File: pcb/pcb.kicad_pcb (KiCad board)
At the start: 2 copper layers, 168.9 x 103.7 mm, 129 parts, among them J1 MJ-4PP-9, J2 MJ-4PP-9, J3 USB_C_Receptacle_USB2.0_16P, J4 USB to TTL, J5 Conn_01x03, J6 Conn_01x03, SW1 KEY_SW, SW10 KEY_SW, SW11 KEY_SW, SW12 KEY_SW, SW13 KEY_SW, SW14 KEY_SW, SW15 KEY_SW, SW16 KEY_SW, SW17 KEY_SW, SW18 KEY_SW, SW19 KEY_SW, SW2 KEY_SW, SW20 KEY_SW, SW21 KEY_SW, SW22 KEY_SW, SW23 KEY_SW, SW24 KEY_SW, SW25 KEY_SW, SW26 KEY_SW, SW27 RotaryEncoder, SW3 KEY_SW, SW30 KEY_SW, SW31 KEY_SW, SW32 KEY_SW, SW33 KEY_SW, SW34 KEY_SW, SW35 KEY_SW, SW36 KEY_SW, SW37 KEY_SW, SW38 KEY_SW, SW39 KEY_SW, SW4 KEY_SW, SW40 KEY_SW, SW41 KEY_SW, SW42 KEY_SW, SW43 KEY_SW, SW44 KEY_SW, SW45 KEY_SW, SW46 KEY_SW, SW47 KEY_SW, SW48 KEY_SW, SW49 KEY_SW, SW5 KEY_SW, SW50 KEY_SW, SW51 KEY_SW, SW52 KEY_SW, SW53 KEY_SW, SW54 KEY_SW, SW6 KEY_SW, SW60 RESET_SW, SW61 BOOT_SW, SW7 KEY_SW, SW8 KEY_SW, SW9 KEY_SW, SW６２1 DIP_SW, U1 ESP32-S3-WROOM-1, U2 TPS1117LV33S, U3 USBLC6-2SC6

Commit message: ortder pcb
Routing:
- net GND: vias 39 -> 45
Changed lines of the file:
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@@
 		(allow_soldermask_bridges_in_footprints no)
 		(aux_axis_origin 232.454776 63.317318)
-		(grid_origin 108.645 50.033114)
+		(grid_origin 111.684776 43.117318)
 		(pcbplotparams
 			(layerselection 0x00010fc_ffffffff)
@@
 			(drillshape 0)
 			(scaleselection 1)
-			(outputdirectory "/home/sotaro/Downloads/")
+			(outputdirectory "../voidaster/")
 		)
 	)
@@
 		(layer "B.SilkS")
 	)
+	(gr_rect
+		(start 107.214776 43.117318)
+		(end 116.154776 50.467318)
+		(stroke
+			(width 0.1)
+			(type solid)
+		)
+		(fill solid)
+		(layer "B.SilkS")
+	)
 	(gr_line
 		(start 180.915 75.502511)
@@
 		(layer "B.SilkS")
 	)
+	(gr_rect
+		(start 107.214776 43.117318)
+		(end 116.154776 50.467318)
+		(stroke
+			(width 0.1)
+			(type solid)
+		)
+		(fill solid)
+		(layer "F.SilkS")
+	)
 	(gr_line
 		(start 124.67977 72.692318)
@@
 	)
 	(via
+		(at 132.174776 51.637318)
+		(size 0.6)
+		(drill 0.3)
+		(layers "F.Cu" "B.Cu")
+		(free yes)
+		(net 34)
+	)
+	(via
 		(at 194.455 95.713114)
 		(size 0.6)
@@
 	)
 	(via
+		(at 165.704776 51.767318)
+		(size 0.6)
+		(drill 0.3)
+		(layers "F.Cu" "B.Cu")
+		(free yes)
+		(net 34)
+	)
+	(via
 		(at 165.885 108.353114)
 		(size 0.6)
@@
 	)
 	(via
+		(at 169.734776 51.747318)
+		(size 0.6)
+		(drill 0.3)
+		(layers "F.Cu" "B.Cu")
+		(free yes)
+		(net 34)
+	)
+	(via
+		(at 137.284776 51.637318)
+		(size 0.6)
+		(drill 0.3)
+		(layers "F.Cu" "B.Cu")
+		(free yes)
+		(net 34)
+	)
+	(via
 		(at 118.035 115.043114)
 		(size 0.6)
@@
 		(net 34)
 	)
+	(via
+		(at 127.774776 51.577318)
+		(size 0.6)
+		(drill 0.3)
+		(layers "F.Cu" "B.Cu")
+		(free yes)
+		(net 34)
+	)
+	(via
+		(at 162.124776 51.837318)
+		(size 0.6)
+		(drill 0.3)
+		(layers "F.Cu" "B.Cu")
+		(free yes)
+		(net 34)
+	)

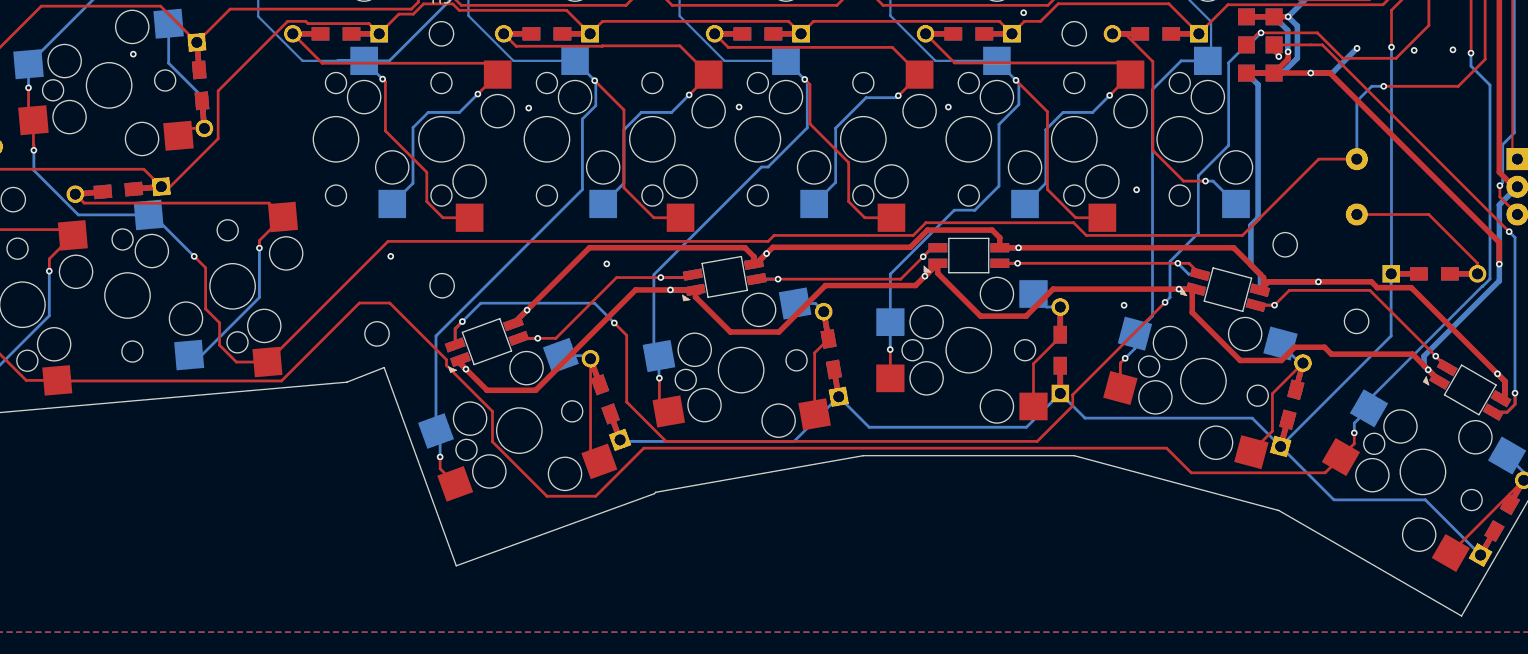
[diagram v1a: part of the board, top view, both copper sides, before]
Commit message: add alphabet at keytop
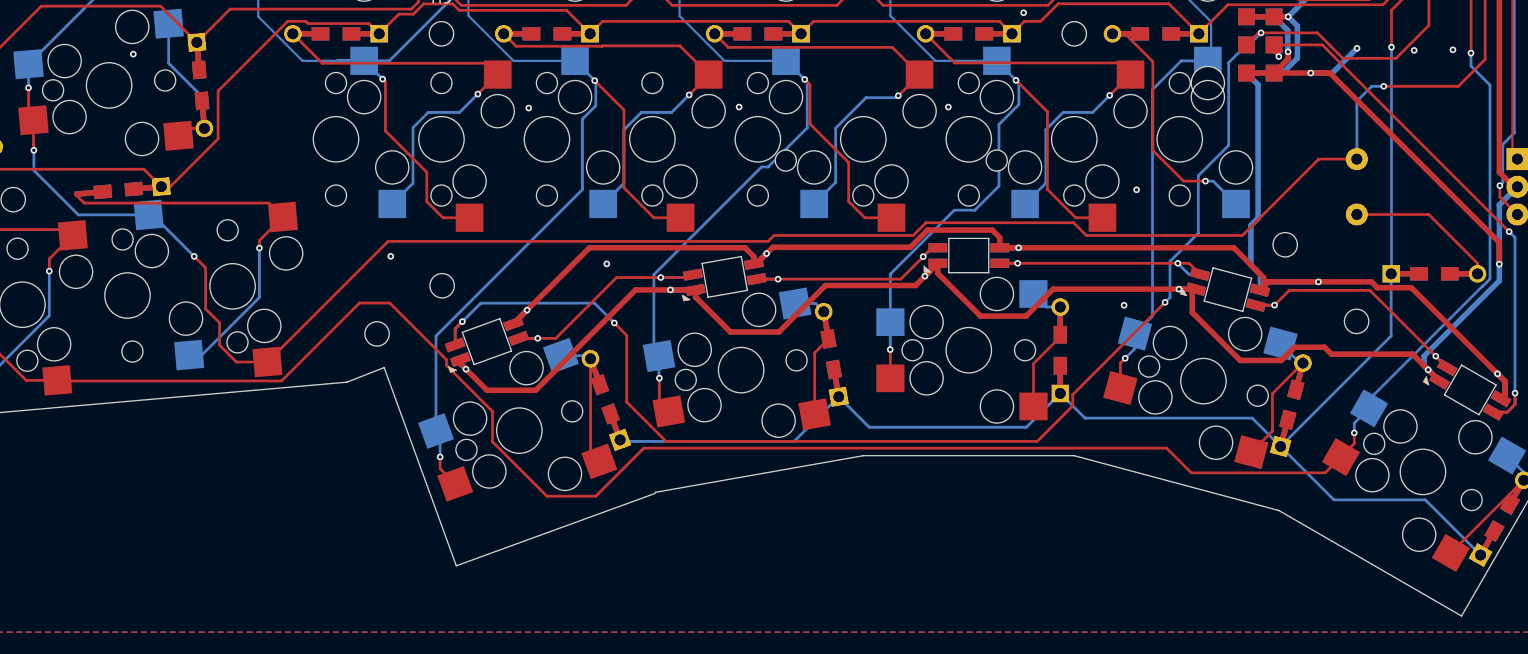
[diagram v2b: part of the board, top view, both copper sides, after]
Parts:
- added ?: , , F.Cu at (172.3, 98.7)
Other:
- board text added: "1"
- board text added: "2"
- board text added: "3"
- board text added: "4"
- board text added: "5"
- board text added: "A"
- board text added: "Alt"
- board text added: "B"
- board text added: "C"
- board text added: "Ctrl"
- board text added: "D"
- board text added: "E"
- board text added: "Esc"
- board text added: "F"
- board text added: "Fn"
- board text added: "G"
- board text added: "Q"
- board text added: "R"
- board text added: "S"
- board text added: "Shif"
- board text added: "T"
- board text added: "Tab"
- board text added: "V"
- board text added: "W"
- board text added: "X"
- board text added: "Z"
